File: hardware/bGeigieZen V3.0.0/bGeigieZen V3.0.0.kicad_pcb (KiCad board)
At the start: 2 copper layers, 129.4 x 64.6 mm, 18 parts, among them J1 M5 2x15 pin, J10 QI GND, J11 QI charger Plus, J2 Geiger IRover, J3 GPS, J4 Geiger Safepulse, J5 Extra support header, J6 Grove, J8 QI charger ground, J9 QI Plus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

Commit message: Updated board a bit more
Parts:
- removed Logo: LOGO, bGeigieRaku_M5_1015:18650 map
- moved J6 39.1 mm to (158.4, 120.2), turned to 180 degrees
- moved G back 5.23 mm to (96.1, 100.3)
- moved J11 4.40 mm to (182.7, 105.1)
- moved J8 3.87 mm to (182.7, 90.2)
- moved J3 2.42 mm to (153.0, 98.5)
- moved J9 2.00 mm to (210.0, 105.0)
- moved J10 1.98 mm to (210.0, 90.5)
- moved SW1 1.93 mm to (184.5, 73.8)
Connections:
- BT1 pad BAT Neg: (no net) -> Net-(BT1--)
- J6 pad 1: GND -> /SCL
- J6 pad 2: 3.3V -> /SDA
- J6 pad 3: /SDA -> 3.3V
- J6 pad 4: /SCL -> GND
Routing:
- net /SDA: track 84.3 -> 40.8 mm
- net /SCL: track 79.1 -> 39.0 mm
- net /GIO2 on Core and GIO32 on Core-2: track 106.0 -> 137.1 mm, vias 0 -> 1
- net 3.3V: track 128.7 -> 119.3 mm
- net /VBATT: track 63.1 -> 66.4 mm
- net Net-(BT1--): track 52.8 -> 49.9 mm, vias 0 -> 1
- net Net-(J9-Pin_1): track 0.00 -> 2.54 mm
- net /RX2: track 44.0 -> 42.4 mm
- net /TX2: track 53.1 -> 51.9 mm
- net /BAT: track 95.4 -> 96.5 mm
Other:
- board text removed: "-"
- board text removed: "IRover"

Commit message: added I2C to GPS bus . Louis idea.
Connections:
- BT1 pad BAT Neg: Net-(BT1--) -> (no net)
- J3 pad 1: unconnected-(J3-Pin_1-Pad1) -> /SDA
- J3 pad 6: unconnected-(J3-Pin_6-Pad6) -> /SCL
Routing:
- net /SCL: track 39.0 -> 93.7 mm
- net /SDA: track 40.8 -> 83.9 mm

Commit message: Rolled back the I2C on the GPS
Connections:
- J3 pad 1: /SDA -> unconnected-(J3-Pin_1-Pad1)
- J3 pad 6: /SCL -> unconnected-(J3-Pin_6-Pad6)
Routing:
- net /SCL: track 93.7 -> 39.0 mm
- net /SDA: track 83.9 -> 40.8 mm
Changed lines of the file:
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@@
   (net 33 "unconnected-(J1-Pin_24-Pad24)")
   (net 34 "unconnected-(J1-Pin_5-Pad5)")
+  (net 35 "unconnected-(J3-Pin_1-Pad1)")
+  (net 36 "unconnected-(J3-Pin_6-Pad6)")
   (footprint "bGeigieZen:LOGO" locked (layer "F.Cu")
     (at 91.1076 100.23 90)
@@
     )
     (pad "1" thru_hole rect (at 0 0 180) (size 1.7 1.7) (drill 1) (layers "*.Cu" "*.Mask")
-      (net 26 "/SDA") (pinfunction "Pin_1") (pintype "passive")
+      (net 35 "unconnected-(J3-Pin_1-Pad1)") (pinfunction "Pin_1") (pintype "passive")
     )
     (pad "2" thru_hole oval (at 0 2.54 180) (size 1.7 1.7) (drill 1) (layers "*.Cu" "*.Mask")
@@
     )
     (pad "6" thru_hole oval (at 0 12.7 180) (size 1.7 1.7) (drill 1) (layers "*.Cu" "*.Mask")
-      (net 27 "/SCL") (pinfunction "Pin_6") (pintype "passive")
+      (net 36 "unconnected-(J3-Pin_6-Pad6)") (pinfunction "Pin_6") (pintype "passive")
     )
     (model "${KICAD6_3DMODEL_DIR}/Connector_PinSocket_2.54mm.3dshapes/PinSocket_1x06_P2.54mm_Vertical.wrl"
@@
   (segment (start 193.608 90.47) (end 194.253 91.1148) (width 0.25) (layer "B.Cu") (net 19))
   (segment (start 193.6076 90.47) (end 193.608 90.47) (width 0.25) (layer "B.Cu") (net 19))
-  (segment (start 121.1326 116.407) (end 121.1326 109.893648) (width 0.25) (layer "F.Cu") (net 26))
   (segment (start 128.551 120.437) (end 148.439 120.437) (width 0.25) (layer "F.Cu") (net 26))
   (segment (start 158.4476 118.169) (end 158.448 118.169) (width 0.25) (layer "F.Cu") (net 26))
@@
   (segment (start 127.483 118.471) (end 127.483 119.369) (width 0.25) (layer "F.Cu") (net 26))
   (segment (start 126.596 117.584) (end 127.483 118.471) (width 0.25) (layer "F.Cu") (net 26))
-  (segment (start 132.526248 98.5) (end 152.9846 98.5) (width 0.25) (layer "F.Cu") (net 26))
   (segment (start 121.133 116.407) (end 121.1326 116.407) (width 0.25) (layer "F.Cu") (net 26))
   (segment (start 122.309 116.407) (end 122.309 116.775) (width 0.25) (layer "F.Cu") (net 26))
@@
   (segment (start 121.133 116.407) (end 122.309 116.407) (width 0.25) (layer "F.Cu") (net 26))
   (segment (start 122.309 116.775) (end 123.118 117.584) (width 0.25) (layer "F.Cu") (net 26))
-  (segment (start 121.1326 109.893648) (end 132.526248 98.5) (width 0.25) (layer "F.Cu") (net 26))
-  (segment (start 119.9388 106.6788) (end 140.7668 85.9016) (width 0.25) (layer "F.Cu") (net 27))
-  (segment (start 121.1326 118.947) (end 119.9388 118.312) (width 0.25) (layer "F.Cu") (net 27))
   (segment (start 157.446 120.169) (end 158.4476 120.169) (width 0.25) (layer "F.Cu") (net 27))
   (segment (start 156.226 121.389) (end 157.446 120.169) (width 0.25) (layer "F.Cu") (net 27))
@@
   (segment (start 122.309 119.315) (end 124.384 121.389) (width 0.25) (layer "F.Cu") (net 27))
   (segment (start 122.309 118.947) (end 122.309 119.315) (width 0.25) (layer "F.Cu") (net 27))
-  (segment (start 140.7668 85.9016) (end 152.9846 85.8) (width 0.25) (layer "F.Cu") (net 27))
-  (segment (start 119.9388 118.312) (end 119.9388 106.6788) (width 0.25) (layer "F.Cu") (net 27))
   (segment (start 121.133 118.947) (end 121.1326 118.947) (width 0.25) (layer "F.Cu") (net 27))
   (segment (start 207.498 104.977) (end 207.4976 104.977) (width 0.25) (layer "F.Cu") (net 29))

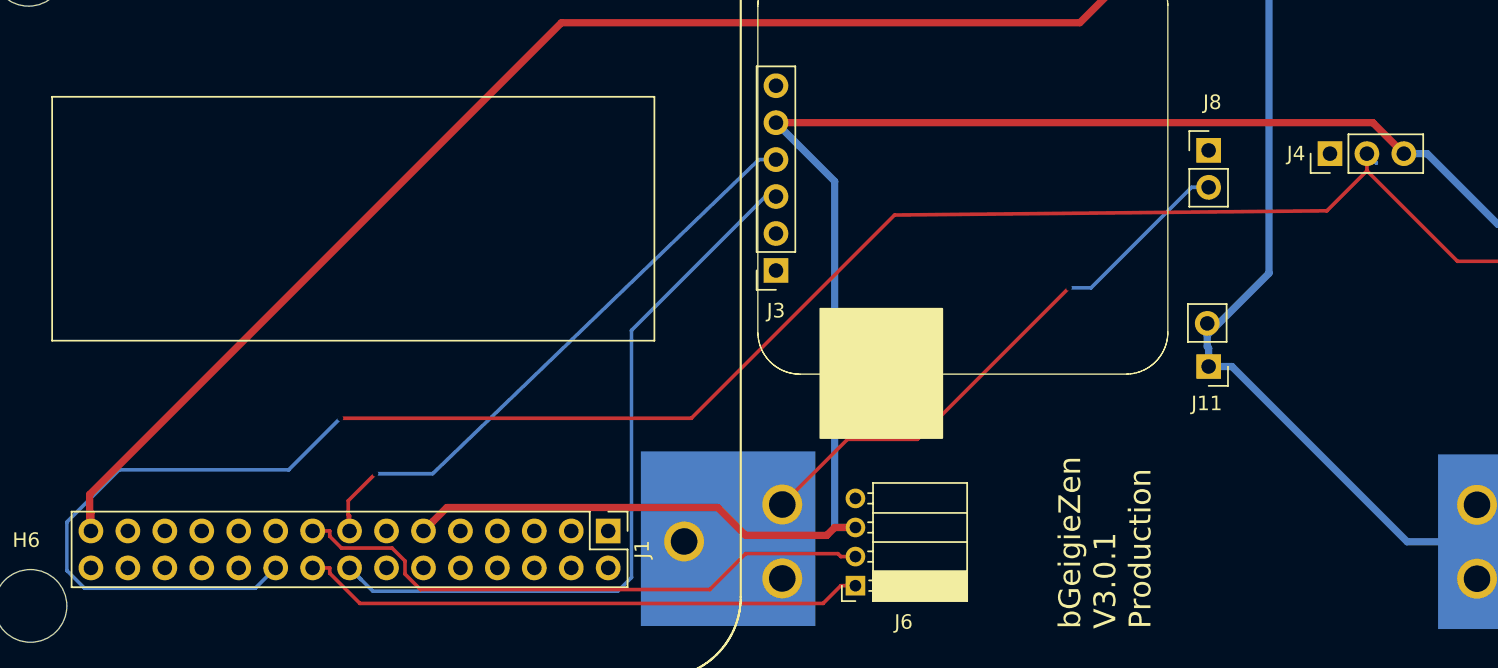
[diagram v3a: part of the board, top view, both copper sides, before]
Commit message: Updated V3.0.1 production board
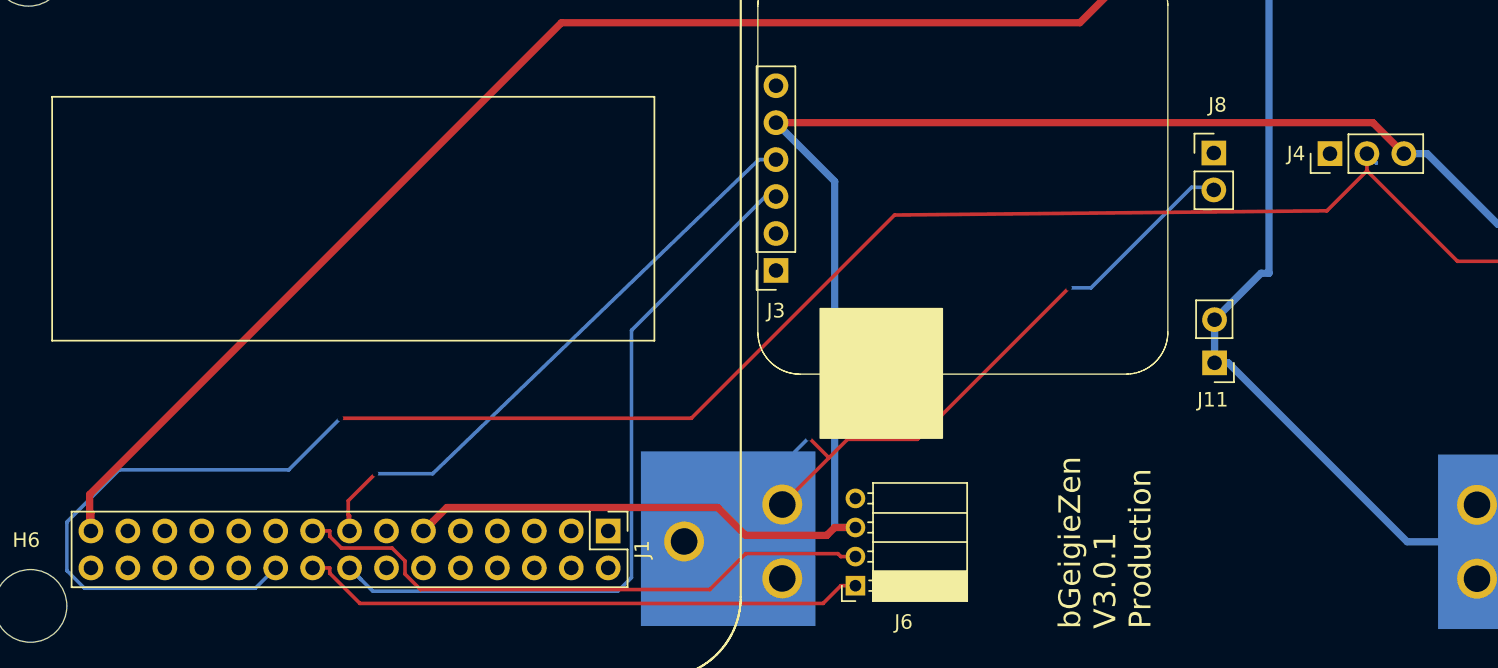
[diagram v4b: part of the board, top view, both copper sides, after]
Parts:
- moved J11 0.48 mm to (183.1, 104.8)
- moved J8 0.40 mm to (183.1, 90.4)
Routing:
- net Net-(BT1--): track 49.9 -> 60.0 mm, vias 1 -> 2
- net /VBATT: track 66.4 -> 64.4 mm
